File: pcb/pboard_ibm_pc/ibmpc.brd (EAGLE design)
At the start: 56 x 65 mm, 49 parts, among them IC1 STM32F072C8T6, SW1 324_SW, SW4 324_SW, U1 MAX3232

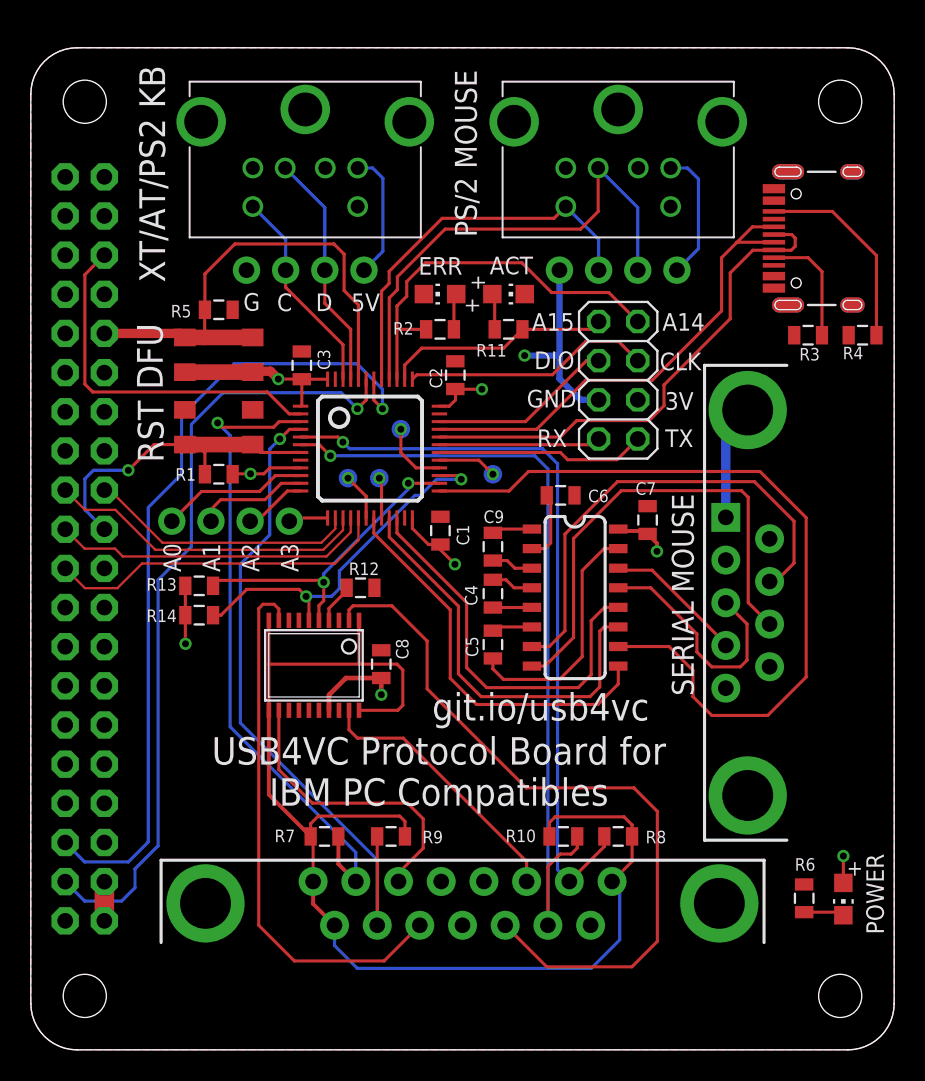
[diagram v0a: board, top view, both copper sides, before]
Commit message: finished ADB protocol board
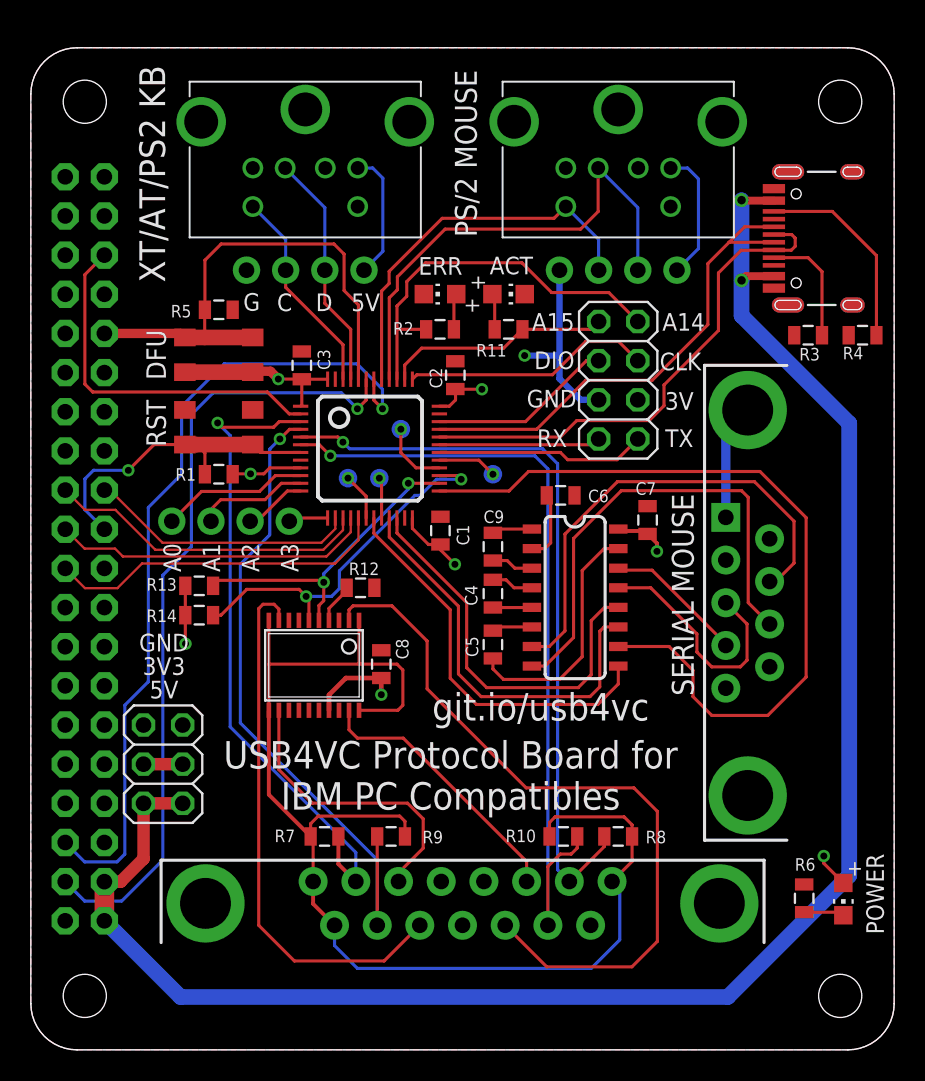
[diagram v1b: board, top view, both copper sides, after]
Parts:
- added JP2: (no value), pinhead:2X03
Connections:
- net +3V3: now also JP2.3, JP2.4
- net +5V: now also J4.VBUS1, J4.VBUS2, JP2.1, JP2.2
- net GND: now also JP2.5, JP2.6
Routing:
- net +5V: track 2.54 -> 116.5 mm, vias 0 -> 2
- net +3V3: track 39.0 -> 42.0 mm
- net N$8: track 31.6 -> 32.4 mm
- net N$18: track 32.5 -> 33.0 mm
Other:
- board text added: "3V3"

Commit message: added dsub stacker board
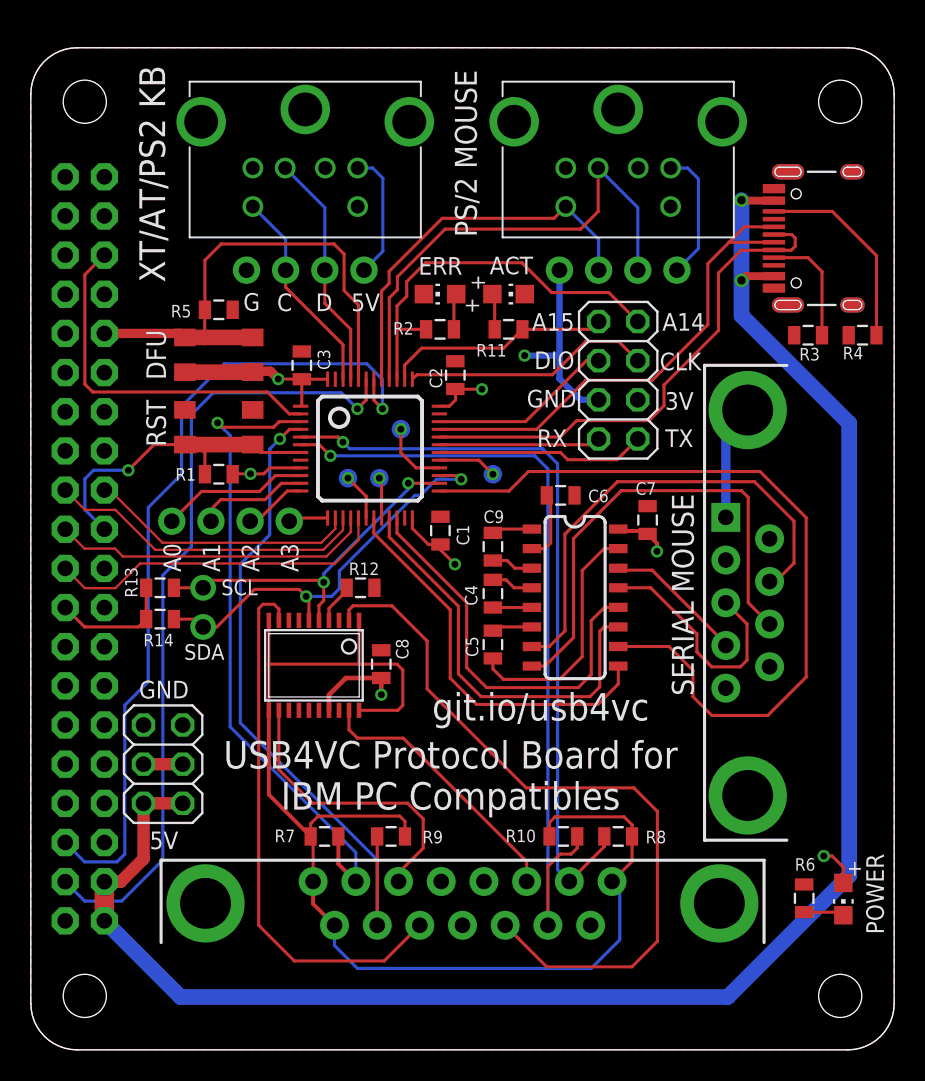
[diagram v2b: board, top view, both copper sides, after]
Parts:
- added U$10: PINHD1X2, adafruit_changed:1X02
- moved R14 2.55 mm to (8.38, 27.9)
- moved R13 2.54 mm to (8.38, 30.0)
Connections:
- removed net N$30: IC1.27, R14.2, U$6.6
- removed net N$31: IC1.26, R13.2, U$6.5
- new net POT_SCL: IC1.26, R13.2, U$10.2, U$6.5
- new net PST_SDA: IC1.27, R14.2, U$10.1, U$6.6
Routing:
- net PST_SDA: track 0.00 -> 27.0 mm, vias 0 -> 2
- net N$30: track 23.9 -> 0.00 mm, vias 2 -> 0
- net POT_SCL: track 0.00 -> 23.3 mm, vias 0 -> 2
- net N$31: track 20.7 -> 0.00 mm, vias 2 -> 0
- net +3V3: track 42.0 -> 46.6 mm, vias 8 -> 7
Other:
- board text added: "SCL"
- board text added: "SDA"
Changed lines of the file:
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@@
 PT1 dekuNukem Dec 2021</text>
 <text x="33.0708" y="22.2504" size="1.778" layer="25" rot="R180" align="center">git.io/usb4vc</text>
-<text x="8.636" y="26.416" size="1.143" layer="25" rot="R180" align="center">GND</text>
-<text x="8.636" y="23.368" size="1.143" layer="25" align="center">5V</text>
-<text x="8.636" y="24.892" size="1.143" layer="25" rot="R180" align="center">3V3</text>
+<text x="8.636" y="23.368" size="1.143" layer="25" rot="R180" align="center">GND</text>
+<text x="8.636" y="13.589" size="1.143" layer="25" align="center">5V</text>
+<text x="12.7" y="18.542" size="1.143" layer="26" rot="MR180" align="center">3V3</text>
+<text x="13.5382" y="29.9974" size="1.016" layer="25" align="center">SCL</text>
+<text x="11.2522" y="25.8064" size="1.016" layer="25" align="center">SDA</text>
+<text x="12.7" y="21.082" size="1.143" layer="26" rot="MR180" align="center">GND</text>
+<text x="12.7" y="16.002" size="1.143" layer="26" rot="MR0" align="center">5V</text>
 </plain>
 <attributes>
@@
 </element>
 <element name="U$6" library="ps2" package="TSSOP20" value="MCP4451" x="18.3642" y="24.9428" smashed="yes" rot="R180">
-<attribute name="VALUE" x="13.066" y="28.0162" size="1.016" layer="27" font="vector" ratio="10" rot="R270"/>
+<attribute name="VALUE" x="13.701" y="28.1432" size="1.016" layer="27" font="vector" ratio="10" rot="R270"/>
 </element>
 <element name="U$7" library="adafruit_changed" package="1X04-CLEANBIG" value="PINHD1X4" x="38.1" y="50.5748" smashed="yes" rot="R180"/>
@@
 <attribute name="TP_SIGNAL_NAME" value="" x="22.606" y="37.084" size="1.778" layer="28" rot="MR0" display="off"/>
 </element>
-<element name="R13" library="SparkFun-Passives" package="0805" value="5.1k" x="10.922" y="30.099" smashed="yes">
-<attribute name="NAME" x="7.493" y="29.7815" size="0.8128" layer="25"/>
-</element>
-<element name="R14" library="SparkFun-Passives" package="0805" value="5.1k" x="10.922" y="28.194" smashed="yes">
-<attribute name="NAME" x="7.493" y="27.7495" size="0.8128" layer="25"/>
+<element name="R13" library="SparkFun-Passives" package="0805" value="5.1k" x="8.382" y="29.972" smashed="yes">
+<attribute name="NAME" x="6.9215" y="29.337" size="0.8128" layer="25" rot="R90"/>
+</element>
+<element name="R14" library="SparkFun-Passives" package="0805" value="5.1k" x="8.382" y="27.94" smashed="yes">
+<attribute name="NAME" x="9.271" y="26.9875" size="0.8128" layer="25" rot="R180"/>
 </element>
 <element name="JP2" library="pinhead" library_urn="urn:adsk.eagle:library:325" package="2X03" package3d_urn="urn:adsk.eagle:package:22462/2" value="" x="8.58" y="18.53" smashed="yes" rot="R90">
@@
 <attribute name="VALUE" x="11.755" y="14.72" size="1.27" layer="27" rot="R90"/>
 </element>
+<element name="U$10" library="adafruit_changed" package="1X02" value="PINHD1X2" x="11.176" y="28.702" smashed="yes" rot="R90"/>
 </elements>
 <signals>
@@
 <wire x1="20.436" y1="24.119" x2="19.3392" y2="23.0222" width="0.3048" layer="1"/>
 <via x="51.435" y="12.573" extent="1-16" drill="0.45"/>
-<wire x1="51.435" y1="12.573" x2="51.435" y2="12.099" width="0.2032" layer="1"/>
-<wire x1="51.435" y1="12.099" x2="52.705" y2="10.829" width="0.2032" layer="1"/>
+<wire x1="51.435" y1="12.573" x2="51.977" y2="12.573" width="0.2032" layer="1"/>
+<wire x1="52.705" y1="11.845" x2="51.977" y2="12.573" width="0.2032" layer="1"/>
+<wire x1="52.705" y1="11.845" x2="52.705" y2="10.829" width="0.2032" layer="1"/>
 <wire x1="38.106" y1="33.782" x2="38.354" y2="33.782" width="0.254" layer="1"/>
 <wire x1="38.354" y1="33.782" x2="38.481" y2="33.655" width="0.254" layer="1"/>
@@
 <contactref element="R13" pad="1"/>
 <contactref element="R14" pad="1"/>
-<via x="10.033" y="26.3398" extent="1-16" drill="0.45"/>
-<wire x1="10.033" y1="26.3398" x2="10.022" y2="26.3508" width="0.2032" layer="1"/>
-<wire x1="10.022" y1="26.3508" x2="10.022" y2="28.194" width="0.2032" layer="1"/>
-<wire x1="10.022" y1="28.194" x2="10.022" y2="30.099" width="0.2032" layer="1"/>
 <contactref element="JP2" pad="3"/>
 <contactref element="JP2" pad="4"/>
 <wire x1="9.85" y1="18.53" x2="7.31" y2="18.53" width="0.8128" layer="1"/>
+<wire x1="2.23" y1="28.69" x2="3.488" y2="27.432" width="0.2032" layer="1"/>
+<wire x1="6.974" y1="27.432" x2="7.482" y2="27.94" width="0.2032" layer="1"/>
+<wire x1="3.488" y1="27.432" x2="6.974" y2="27.432" width="0.2032" layer="1"/>
+<wire x1="7.482" y1="27.94" x2="7.482" y2="29.972" width="0.2032" layer="1"/>
 </signal>
 <signal name="N$29">
@@
 <wire x1="3.5134" y1="29.9466" x2="2.23" y2="31.23" width="0.1524" layer="1"/>
 <wire x1="21.25" y1="34.5" x2="21.25" y2="33.061" width="0.1524" layer="1"/>
-<wire x1="5.6134" y1="29.9466" x2="3.5134" y2="29.9466" width="0.1524" layer="1"/>
+<wire x1="5.4864" y1="29.9466" x2="3.5134" y2="29.9466" width="0.1524" layer="1"/>
 <wire x1="21.25" y1="33.061" x2="19.7358" y2="31.5468" width="0.1524" layer="1"/>
-<wire x1="19.7358" y1="31.5468" x2="7.2136" y2="31.5468" width="0.1524" layer="1"/>
-<wire x1="7.2136" y1="31.5468" x2="5.6134" y2="29.9466" width="0.1524" layer="1"/>
+<wire x1="19.7358" y1="31.5468" x2="7.0866" y2="31.5468" width="0.1524" layer="1"/>
+<wire x1="7.0866" y1="31.5468" x2="5.4864" y2="29.9466" width="0.1524" layer="1"/>
 </signal>
 <signal name="N$1">
@@
 <wire x1="22.25" y1="42.139" x2="22.8092" y2="41.5798" width="0.2032" layer="1"/>
 <via x="22.8092" y="41.5798" extent="1-16" drill="0.45"/>
-<wire x1="22.8092" y1="41.5798" x2="22.8092" y2="42.8498" width="0.2032" layer="16"/>
-<wire x1="22.8092" y1="42.8498" x2="21.1582" y2="44.5008" width="0.2032" layer="16"/>
+<wire x1="22.8092" y1="41.5798" x2="22.8092" y2="43.4848" width="0.2032" layer="16"/>
+<wire x1="22.8092" y1="43.4848" x2="21.7932" y2="44.5008" width="0.2032" layer="16"/>
 <wire x1="3.488" y1="12.192" x2="2.23" y2="13.45" width="0.2032" layer="16"/>
-<wire x1="21.1582" y1="44.5008" x2="12.5476" y2="44.5008" width="0.2032" layer="16"/>
+<wire x1="21.7932" y1="44.5008" x2="12.5476" y2="44.5008" width="0.2032" layer="16"/>
 <wire x1="12.5476" y1="44.5008" x2="9.779" y2="41.7322" width="0.2032" layer="16"/>
 <wire x1="9.779" y1="37.338" x2="7.62" y2="35.179" width="0.2032" layer="16"/>
@@
 <wire x1="30.088" y1="48.872" x2="30.088" y2="46.736" width="0.2032" layer="1"/>
 </signal>
-<signal name="N$30">
+<signal name="PST_SDA">
 <contactref element="IC1" pad="27"/>
 <contactref element="U$6" pad="6"/>
@@
 <contactref element="R14" pad="2"/>
 <wire x1="17.8562" y1="29.4132" x2="17.399" y2="29.8704" width="0.2032" layer="1"/>
-<wire x1="17.399" y1="29.8704" x2="14.0064" y2="29.8704" width="0.2032" layer="1"/>
-<wire x1="14.0064" y1="29.8704" x2="12.33" y2="28.194" width="0.2032" layer="1"/>
-<wire x1="12.33" y1="28.194" x2="11.822" y2="28.194" width="0.2032" layer="1"/>
-</signal>
-<signal name="N$31">
+<contactref element="U$10" pad="1"/>
+<wire x1="17.399" y1="29.8704" x2="14.5034" y2="29.8704" width="0.2032" layer="1"/>
+<wire x1="12.065" y1="27.432" x2="11.176" y2="27.432" width="0.2032" layer="1"/>
+<wire x1="14.5034" y1="29.8704" x2="12.065" y2="27.432" width="0.2032" layer="1"/>
+<wire x1="9.282" y1="27.94" x2="10.668" y2="27.94" width="0.2032" layer="1"/>
+<wire x1="10.668" y1="27.94" x2="11.176" y2="27.432" width="0.2032" layer="1"/>
+</signal>
+<signal name="POT_SCL">
 <contactref element="IC1" pad="26"/>
 <contactref element="U$6" pad="5"/>
@@
 <contactref element="R13" pad="2"/>
 <wire x1="18.9992" y1="30.3276" x2="18.8722" y2="30.4546" width="0.2032" layer="1"/>
-<wire x1="18.8722" y1="30.4546" x2="12.1776" y2="30.4546" width="0.2032" layer="1"/>
-<wire x1="12.1776" y1="30.4546" x2="11.822" y2="30.099" width="0.2032" layer="1"/>
+<contactref element="U$10" pad="2"/>
+<wire x1="18.8722" y1="30.4546" x2="11.6586" y2="30.4546" width="0.2032" layer="1"/>
+<wire x1="11.6586" y1="30.4546" x2="11.176" y2="29.972" width="0.2032" layer="1"/>
+<wire x1="11.176" y1="29.972" x2="9.282" y2="29.972" width="0.2032" layer="1"/>
 </signal>
 <signal name="N$32">

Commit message: finishing touches for new boards
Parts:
- removed SW4: 324_SW, 3pos_slide_switch_centered:342_SWICH_FOOT
- removed TP4: TPTP12R, testpad:TP12R
- added R15: 2K, SparkFun-Passives:0805
- added SW2: 324_SW, 3pos_slide_switch_centered:342_SWICH_FOOT
- C3: value 1uF -> 100nF
- C9: value 100nF -> 1uF
- J2: device SparkFun-Connectors:DIN7 -> SparkFun-Connectors:DB9_MALE
- J3: device SparkFun-Connectors:DB9_MALE -> SparkFun-Connectors:DIN7
- R1: value 12K -> 5.1k
- R11, R9: value 2K -> 12K
- R2: value 2K -> 5.1k
- R3, R4: value 5.1k -> 2K
- R5: value 12K -> 2K
- U$1: value GAMEPORT_15P -> PINHD1X4; device ibmpc:DA15 -> adafruit_changed:1X04-CLEANBIG
- U$10: value PINHD1X2 -> PINHD1X4; device adafruit_changed:1X02 -> adafruit_changed:1X04-CLEANBIG
- U$4: value M2.5HOLE -> PINHD1X2; device f1c100s:M2.5HOLE -> adafruit_changed:1X02
- U$5: value M2.5HOLE -> MCP4451; device f1c100s:M2.5HOLE -> ps2:TSSOP20
- U$6: value MCP4451 -> M2.5HOLE; device ps2:TSSOP20 -> f1c100s:M2.5HOLE
- U$7: value PINHD1X4 -> M2.5HOLE; device adafruit_changed:1X04-CLEANBIG -> f1c100s:M2.5HOLE
- U$9: value PINHD1X4 -> GAMEPORT_15P; device adafruit_changed:1X04-CLEANBIG -> ibmpc:DA15
- moved U$5 50.0 mm to (18.4, 24.9), turned to 180 degrees
- moved R14 48.3 mm to (53.1, 46.4)
- moved LED1 47.2 mm to (52.7, 9.78), turned to 180 degrees
- moved LED2 47.2 mm to (26.5, 49.0), turned to 90 degrees
- moved R13 44.4 mm to (49.7, 46.4), turned to 180 degrees
- moved J2 43.0 mm to (46.5, 29.0), turned to 270 degrees
- moved U$1 42.3 mm to (17.8, 50.6)
- moved R5 42.1 mm to (36.8, 13.8), turned to 0 degrees
- moved R3 41.2 mm to (18.5, 20.3)
- moved U$6 39.5 mm to (3.50, 61.5), turned to 0 degrees
- moved R4 36.5 mm to (21.4, 30.0), turned to 0 degrees
- moved U$4 33.8 mm to (11.2, 28.6), turned to 90 degrees
- moved J3 33.1 mm to (38.1, 61.0), turned to 0 degrees
- moved R7 31.4 mm to (50.2, 9.83), turned to 270 degrees
- moved R6 31.1 mm to (19.3, 13.8), turned to 180 degrees
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- renumbered JP4 to JP3
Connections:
- removed net N$35: U$1.6, U$6.19
- removed net N$36: U$1.13, U$6.2
- new net N$30: U$5.9, U$9.13
- new net N$31: IC1.6, R5.1, U$9.2
- net +3V3: now also C1.1, C6.2, C7.2, C9.2, LED1.A, R1.1, R2.1, R3.1, R9.2, SW2.P$2, SW2.P$3, U$5.17; no longer C1.2, C2.2, C3.2, C7.1, LED2.A, R1.2, R13.1, R14.1, SW1.P$2, SW1.P$3, U$6.17
- net +UB: now also R5.2, R6.2, U$5.1, U$5.10, U$5.11, U$5.20, U$9.1, U$9.8, U$9.9; no longer R7.2, R9.2, U$1.1, U$1.8, U$1.9, U$6.1, U$6.10, U$6.11, U$6.20
- net C1+: now also C3.1; no longer C9.1
- net C1-: now also C3.2; no longer C9.2
- net C2+: now also C5.1; no longer C4.1
- net C2-: now also C5.2; no longer C4.2
- net GND: now also C1.2, C2.2, C4.2, C6.1, C7.1, C9.1, J2.5, J2.G1, J2.G2, J3.3_GND, J3.SHIELD1, J3.SHIELD2, J3.SHIELD3, LED2.C, R11.1, R13.2, R14.2, R7.1, SW1.P$1, SW1.P$4, U$5.16, U$5.7, U$9.4, U$9.5, U$9.G1, U$9.G2; no longer C1.1, C2.1, C3.1, C5.2, C6.2, C7.2, J2.3_GND, J2.SHIELD1, J2.SHIELD2, J2.SHIELD3, J3.5, J3.G1, J3.G2, LED1.C, R12.2, R3.2, R5.1, R6.1, SW4.P$1, SW4.P$4, U$1.5, U$1.G1, U$1.G2, U$6.16, U$6.7, U$7.4
- net N$1: now also R13.1; no longer R3.1
- net N$10: now also J1.1_DATA, U$1.2; no longer J2.1_DATA, U$8.2
- net N$11: now also J1.5_CLK, U$1.3; no longer J2.5_CLK, U$8.3
- net N$13: now also R9.1, SW1.P$2, SW1.P$3; no longer R1.1, SW4.P$2, SW4.P$3
- net N$17: now also U$5.12, U$9.6; no longer IC1.3, R7.1, U$1.2
- net N$18: now also R11.2, SW2.P$1, SW2.P$4; no longer R5.2, SW1.P$1, SW1.P$4
- net N$19: now also IC1.4, R6.1, U$9.7; no longer IC1.5, R8.1, U$1.7
- net N$2: now also LED2.A, R12.2; no longer LED1.A, R2.2
- net N$20: now also IC1.5, R8.1, U$9.10; no longer IC1.4, R9.1, U$1.10
- net N$21: now also IC1.3, U$9.14; no longer IC1.6, U$1.14
- net N$25: now also J2.8; no longer J3.8
- net N$26: now also J3.1_DATA, U$8.2; no longer J1.1_DATA, U$7.2
- net N$27: now also R15.1; no longer R11.1
- net N$28: now also R15.2; no longer R11.2
- net N$29: now also LED1.C, R7.2; no longer LED2.C, R6.2
- net N$3: now also J3.4_5V, U$8.1; no longer J1.4_5V, U$7.1
- net N$32: now also R4.1, U$5.4; no longer R12.1, U$6.4
- net N$33: now also U$5.19, U$9.11; no longer U$1.3, U$6.12
- net N$34: now also U$5.2, U$9.3; no longer U$1.11, U$6.9
- net N$38: now also U$10.1; no longer U$9.1
- net N$39: now also U$10.2; no longer U$9.2
- net N$4: now also J1.4_5V, U$1.1; no longer J2.4_5V, U$8.1
- net N$40: now also U$10.3; no longer U$9.3
- net N$41: now also U$10.4; no longer U$9.4
- net N$44: now also R3.2, U$5.15; no longer TP4.TP
- net N$5: now also J3.5_CLK, U$8.3; no longer J1.5_CLK, U$7.3
- net N$6: now also R12.1; no longer R2.1
- net N$7: now also R14.1; no longer R4.1
- net POT_SCL: now also R1.2, U$4.2, U$5.5; no longer R13.2, U$10.2, U$6.5
- net PST_SDA: now also R2.2, U$4.1, U$5.6; no longer R14.2, U$10.1, U$6.6
- net RTS_HV: now also J2.7; no longer J3.7
- net STM32_RX_HV: now also J2.3; no longer J3.3
- net STM32_TX_HV: now also J2.2; no longer J3.2
- net V+: now also C2.1; no longer C6.1
- net V-: now also C4.1; no longer C5.1
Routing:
- net N$31: track 0.00 -> 55.7 mm, vias 0 -> 1
- net N$36: track 48.2 -> 0.00 mm
- net N$30: track 0.00 -> 34.0 mm
- net N$17: track 42.5 -> 19.9 mm, vias 1 -> 0
- net N$20: track 43.7 -> 63.8 mm
- net N$35: track 17.6 -> 0.00 mm
- net N$44: track 2.64 -> 16.7 mm, vias 1 -> 2
- net GND: track 35.8 -> 49.3 mm, vias 1 -> 0
- net N$34: track 35.2 -> 24.9 mm
- net N$19: track 48.7 -> 42.6 mm
- net +UB: track 82.8 -> 78.5 mm
- net +3V3: track 46.6 -> 48.9 mm
- net N$7: track 13.0 -> 11.2 mm
- net PC_RTS: track 25.8 -> 27.0 mm
- net STM32_RX_HV: track 15.6 -> 15.0 mm
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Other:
- board text added: "USB4VC Protocol Board IBM PC Compatibles"
- board text removed: "B2"

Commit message: before board run
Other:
- board text removed: "USB4VC Protocol Board IBM PC Compatibles"
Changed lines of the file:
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@@
 <wire x1="0" y1="62" x2="0" y2="3" width="0" layer="20"/>
 <wire x1="0" y1="3" x2="3" y2="0" width="0" layer="20" curve="90"/>
-<text x="28" y="17" size="1.778" layer="25" rot="R180" align="center">USB4VC Protocol Board
+<text x="27.5936" y="17.0762" size="1.778" layer="25" rot="R180" align="center">USB4VC Protocol Board for
 IBM PC Compatibles</text>
 <text x="42.0624" y="42.0878" size="1.143" layer="25" rot="R180" align="center">3V</text>

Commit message: gamepad implemented on ibm board, analoge axes doesnt seem to be working correctly
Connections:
- net N$17 renamed Y1_W0
- net N$30 renamed Y2_W1
- net N$33 renamed X2_W2
- net N$34 renamed X1_W3
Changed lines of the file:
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@@
 <wire x1="34.92" y1="10.92" x2="35.93" y2="11.93" width="0.2032" layer="1"/>
 </signal>
-<signal name="N$17">
+<signal name="Y1_W0">
 <contactref element="U$9" pad="6"/>
 <contactref element="U$5" pad="12"/>
@@
 <wire x1="25.654" y1="12.734" x2="23.84" y2="10.92" width="0.2032" layer="1"/>
 </signal>
-<signal name="N$30">
+<signal name="Y2_W1">
 <contactref element="U$5" pad="9"/>
 <contactref element="U$9" pad="13"/>
@@
 <wire x1="15.0876" y1="28.956" x2="14.7574" y2="28.6258" width="0.2032" layer="1"/>
 </signal>
-<signal name="N$33">
+<signal name="X2_W2">
 <contactref element="U$5" pad="19"/>
 <wire x1="20.6392" y1="22.025" x2="20.6392" y2="20.6358" width="0.2032" layer="1"/>
@@
 <wire x1="30.0962" y1="8.08" x2="30.77" y2="8.08" width="0.2032" layer="1"/>
 </signal>
-<signal name="N$34">
+<signal name="X1_W3">
 <contactref element="U$5" pad="2"/>
 <contactref element="U$9" pad="3"/>
